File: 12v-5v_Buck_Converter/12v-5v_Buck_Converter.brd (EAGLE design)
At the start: 44 x 35.2 mm, 22 parts, among them J1 PJ-037A, U1 ZXMN3A01Z, U2 TERMINAL_BLOCK_2P, U3 TERMINAL_BLOCK_2P, U4 TERMINAL_BLOCK_2P, U5 TERMINAL_BLOCK_2P, U6 RT7258GSP

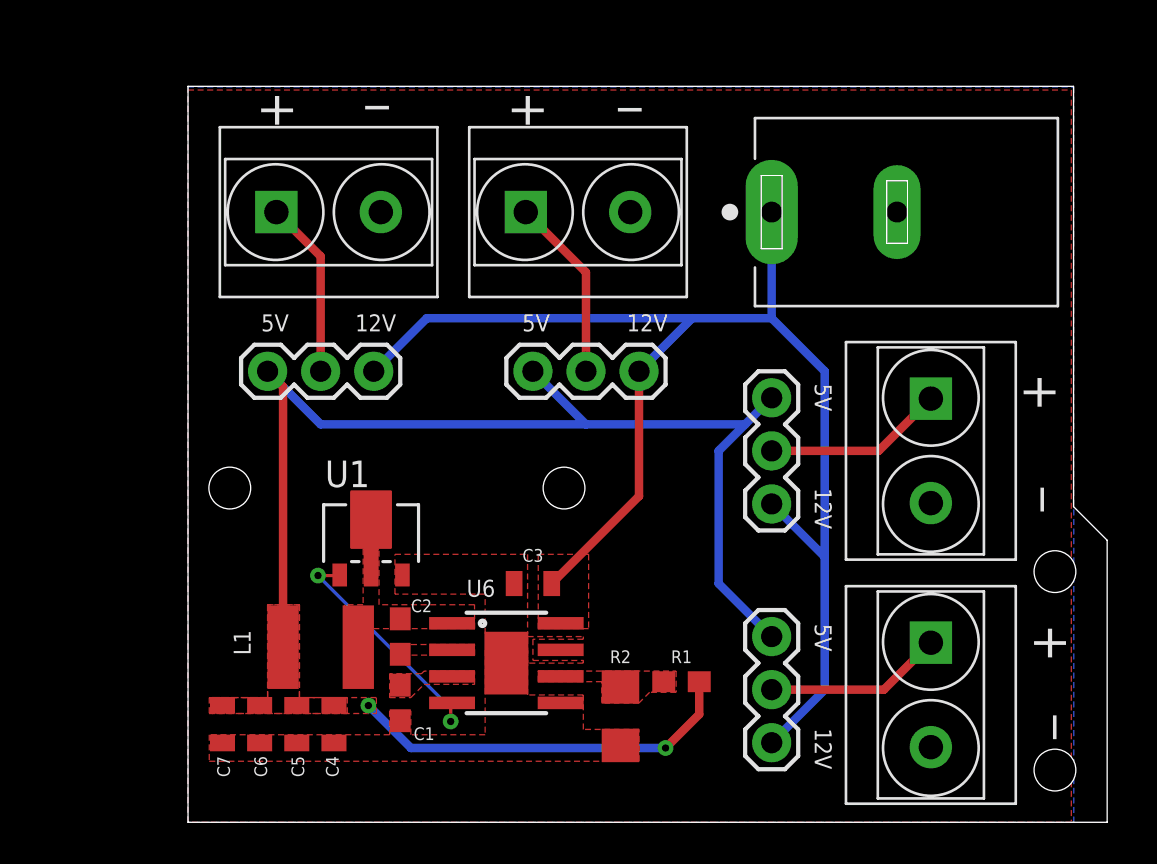
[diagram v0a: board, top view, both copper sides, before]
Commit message: Redesign to fix incorrect specs
MOSFET needed to have a Vgs of 5V and all of the other passive components were adjusted to be more temperature/current compatible
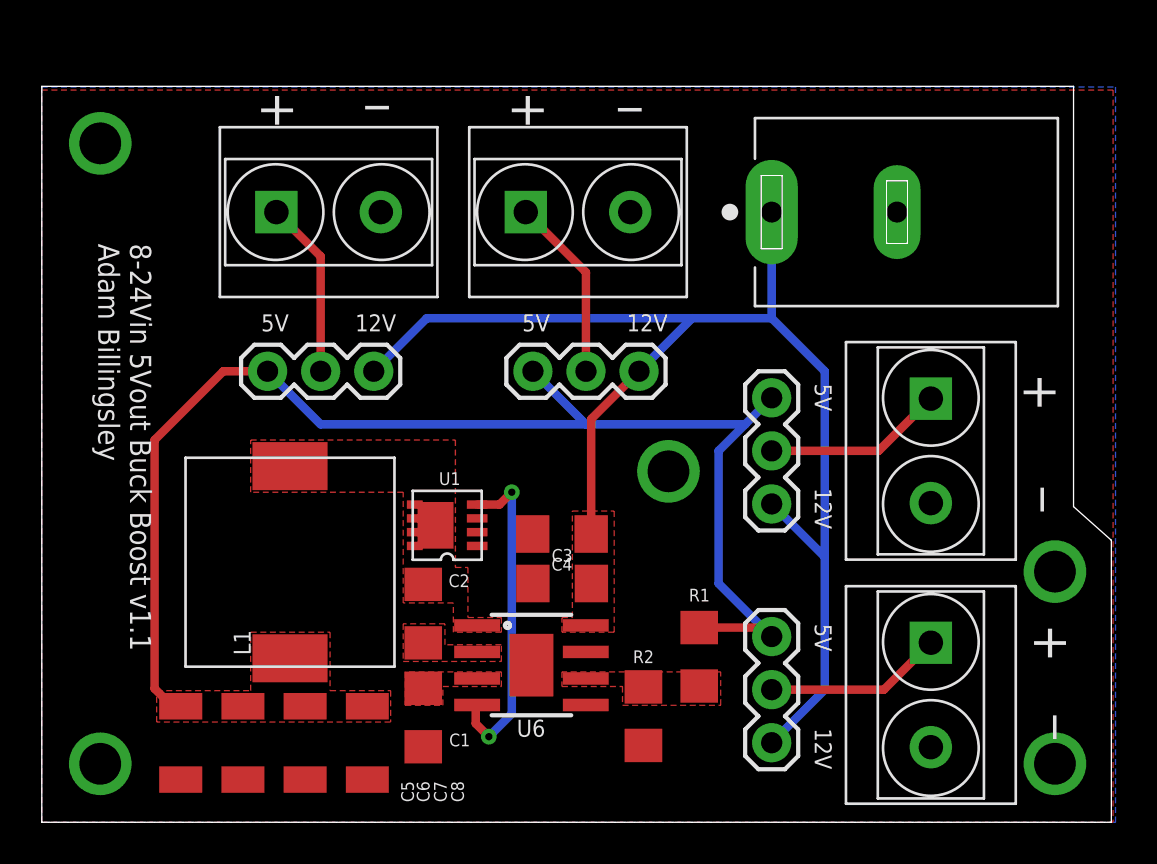
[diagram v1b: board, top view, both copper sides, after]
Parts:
- added C8: 22uF, Adam's Parts (work):1210
- C1, C2: device Adam's Parts (work):0603-CAPACITOR -> Adam's Parts (work):1206-CAPACITOR
- C3, C4: value 22uF -> 10uF; device Adam's Parts (work):0805 -> Adam's Parts (work):1206-CAPACITOR
- C5, C6, C7: device Adam's Parts (work):0805 -> Adam's Parts (work):1210
- L1: value 10uH -> 4.7uH; device Adam's Parts (work):INDUCTOR_LSXND5050YAL100MMG -> Adam's Parts (work):INDUCTOR-7443330470
- R1: value 82k -> 93.1k; device Adam's Parts (work):0603 -> Adam's Parts (work):1206-CAPACITOR
- R2: value 16k -> 18k; device Adam's Parts (work):1206 -> Adam's Parts (work):1206-CAPACITOR
- U1: device Adam's Parts (work):SOT89-R -> Adam's Parts (work):SI7114DN
- moved C4 14.2 mm to (17.9, 13.8), turned to 180 degrees
- moved FRAME1 7.00 mm to (14.0, -8.00)
- moved U1 5.86 mm to (14.3, 15.4), turned to 180 degrees
- moved L1 4.32 mm to (4.88, 12.4), turned to 90 degrees
- moved C5 3.50 mm to (8.59, 3.80)
- moved C6 2.36 mm to (5.61, 3.80)
- moved C2 1.56 mm to (11.3, 9.99)
- moved R1 1.46 mm to (24.5, 7.92), turned to 90 degrees
- moved C3 1.40 mm to (17.9, 11.4)
- moved C7 1.33 mm to (2.63, 3.80)
- moved C1 1.30 mm to (11.3, 5.01)
- moved U6 1.20 mm to (16.4, 7.52)
- moved R2 1.10 mm to (21.8, 5.08)
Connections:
- net 12V: now also C4.1
- net 5V: now also C8.1, L1.2; no longer C4.1, L1.P$2
- net BG: now also U1.4; no longer U1.2
- net GND: now also C8.2, U1.2, U1.3
- net SW: now also L1.1, U1.5, U1.6, U1.7, U1.8, U1.9; no longer L1.P$1, U1.3
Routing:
- net 5V: track 73.5 -> 65.0 mm, vias 2 -> 0
- net BG: track 11.6 -> 15.9 mm
- net 12V: track 66.7 -> 63.5 mm
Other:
- board size 44 x 35.2 mm -> 51.2 x 35.2 mm
- board text added: "8-24Vin 5Vout Buck Boost v1.1 Adam Billingsley"
- board text removed: "12Vin 5Vout Buck Boost v1.0 Adam Billingsley"

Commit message: updated buck converter, added shift register boards
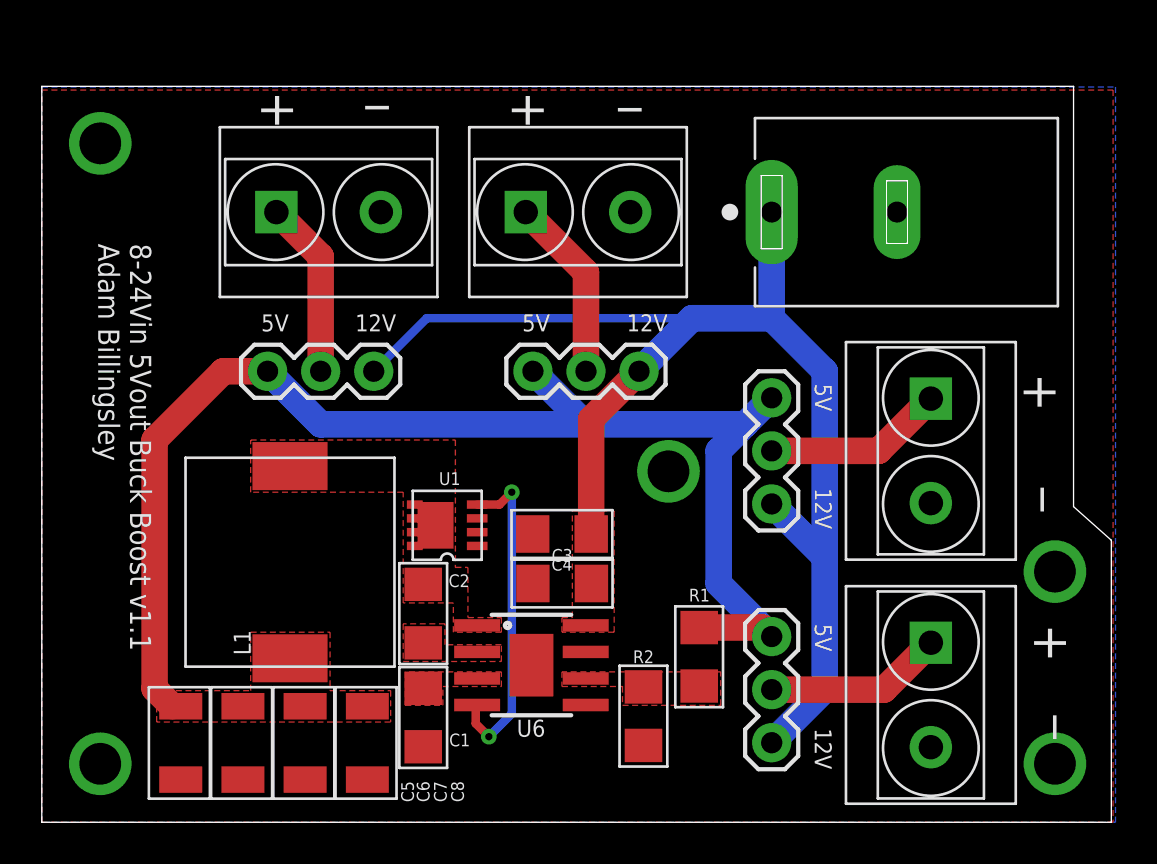
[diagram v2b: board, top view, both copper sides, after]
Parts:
- flipped FRAME1 to the bottom
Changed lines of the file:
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@@
 <layer number="27" name="tValues" color="7" fill="1" visible="yes" active="yes"/>
 <layer number="28" name="bValues" color="7" fill="1" visible="yes" active="yes"/>
-<layer number="29" name="tStop" color="7" fill="3" visible="no" active="yes"/>
-<layer number="30" name="bStop" color="7" fill="6" visible="no" active="yes"/>
-<layer number="31" name="tCream" color="7" fill="4" visible="no" active="yes"/>
-<layer number="32" name="bCream" color="7" fill="5" visible="no" active="yes"/>
-<layer number="33" name="tFinish" color="6" fill="3" visible="no" active="yes"/>
+<layer number="29" name="tStop" color="7" fill="3" visible="yes" active="yes"/>
+<layer number="30" name="bStop" color="7" fill="6" visible="yes" active="yes"/>
+<layer number="31" name="tCream" color="7" fill="4" visible="yes" active="yes"/>
+<layer number="32" name="bCream" color="7" fill="5" visible="yes" active="yes"/>
+<layer number="33" name="tFinish" color="6" fill="3" visible="yes" active="yes"/>
 <layer number="34" name="bFinish" color="6" fill="6" visible="no" active="yes"/>
 <layer number="35" name="tGlue" color="7" fill="4" visible="no" active="yes"/>
@@
 <attribute name="VALUE" x="17.9" y="14.943" size="0.6096" layer="27" font="vector" ratio="20" rot="R180" align="top-center"/>
 </element>
-<element name="FRAME1" library="SparkFun-Aesthetics" library_urn="urn:adsk.eagle:library:507" package="CREATIVE_COMMONS" package3d_urn="urn:adsk.eagle:package:37121/1" value="FRAME-LETTER" x="14" y="-8" smashed="yes"/>
+<element name="FRAME1" library="SparkFun-Aesthetics" library_urn="urn:adsk.eagle:library:507" package="CREATIVE_COMMONS" package3d_urn="urn:adsk.eagle:package:37121/1" value="FRAME-LETTER" x="14" y="-8" smashed="yes" rot="MR0"/>
 </elements>
 <signals>
@@
 <contactref element="JP4" pad="3"/>
 <contactref element="JP3" pad="3"/>
-<wire x1="27.94" y1="20.32" x2="26.67" y2="19.05" width="0.4064" layer="16"/>
-<wire x1="6.35" y1="19.05" x2="3.81" y2="21.59" width="0.4064" layer="16"/>
-<wire x1="26.67" y1="19.05" x2="19.05" y2="19.05" width="0.4064" layer="16"/>
-<wire x1="19.05" y1="19.05" x2="6.35" y2="19.05" width="0.4064" layer="16"/>
-<wire x1="16.51" y1="21.59" x2="19.05" y2="19.05" width="0.4064" layer="16"/>
-<wire x1="27.94" y1="8.89" x2="25.4" y2="11.43" width="0.4064" layer="16"/>
-<wire x1="25.4" y1="11.43" x2="25.4" y2="17.78" width="0.4064" layer="16"/>
-<wire x1="25.4" y1="17.78" x2="26.67" y2="19.05" width="0.4064" layer="16"/>
+<wire x1="27.94" y1="20.32" x2="26.67" y2="19.05" width="1.27" layer="16"/>
+<wire x1="6.35" y1="19.05" x2="3.81" y2="21.59" width="1.27" layer="16"/>
+<wire x1="26.67" y1="19.05" x2="19.05" y2="19.05" width="1.27" layer="16"/>
+<wire x1="19.05" y1="19.05" x2="6.35" y2="19.05" width="1.27" layer="16"/>
+<wire x1="16.51" y1="21.59" x2="19.05" y2="19.05" width="1.27" layer="16"/>
+<wire x1="27.94" y1="8.89" x2="25.4" y2="11.43" width="1.27" layer="16"/>
+<wire x1="25.4" y1="11.43" x2="25.4" y2="17.78" width="1.27" layer="16"/>
+<wire x1="25.4" y1="17.78" x2="26.67" y2="19.05" width="1.27" layer="16"/>
 <polygon width="0.1524" layer="1" thermals="no">
 <vertex x="-1.5" y="4.8"/>
@@
 <vertex x="9.7" y="4.8"/>
 </polygon>
-<wire x1="3.81" y1="21.59" x2="1.69" y2="21.59" width="0.4064" layer="1"/>
-<wire x1="1.69" y1="21.59" x2="-1.6" y2="18.3" width="0.4064" layer="1"/>
-<wire x1="-1.6" y1="18.3" x2="-1.6" y2="6.4" width="0.4064" layer="1"/>
-<wire x1="-1.6" y1="6.4" x2="-0.754" y2="5.554" width="0.4064" layer="1"/>
+<wire x1="3.81" y1="21.59" x2="1.69" y2="21.59" width="1.27" layer="1"/>
+<wire x1="1.69" y1="21.59" x2="-1.6" y2="18.3" width="1.27" layer="1"/>
+<wire x1="-1.6" y1="18.3" x2="-1.6" y2="6.4" width="1.27" layer="1"/>
+<wire x1="-1.6" y1="6.4" x2="-0.754" y2="5.554" width="1.27" layer="1"/>
 <wire x1="-0.754" y1="5.554" x2="-0.349" y2="5.554" width="0.4064" layer="1"/>
-<wire x1="24.469" y1="9.322" x2="27.508" y2="9.322" width="0.4064" layer="1"/>
-<wire x1="27.508" y1="9.322" x2="27.94" y2="8.89" width="0.4064" layer="1"/>
+<wire x1="24.469" y1="9.322" x2="27.508" y2="9.322" width="1.27" layer="1"/>
+<wire x1="27.508" y1="9.322" x2="27.94" y2="8.89" width="1.27" layer="1"/>
 </signal>
 <signal name="BG">
@@
 <contactref element="JP3" pad="1"/>
 <contactref element="JP4" pad="1"/>
-<wire x1="27.94" y1="15.24" x2="30.48" y2="12.7" width="0.4064" layer="16"/>
-<wire x1="30.48" y1="6.35" x2="27.94" y2="3.81" width="0.4064" layer="16"/>
-<wire x1="30.48" y1="12.7" x2="30.48" y2="6.35" width="0.4064" layer="16"/>
-<wire x1="30.48" y1="12.7" x2="30.48" y2="21.59" width="0.4064" layer="16"/>
-<wire x1="30.48" y1="21.59" x2="27.94" y2="24.13" width="0.4064" layer="16"/>
-<wire x1="27.94" y1="24.13" x2="24.13" y2="24.13" width="0.4064" layer="16"/>
-<wire x1="24.13" y1="24.13" x2="21.59" y2="21.59" width="0.4064" layer="16"/>
-<wire x1="27.94" y1="29.21" x2="27.94" y2="24.13" width="0.4064" layer="16"/>
+<wire x1="27.94" y1="15.24" x2="30.48" y2="12.7" width="1.27" layer="16"/>
+<wire x1="30.48" y1="6.35" x2="27.94" y2="3.81" width="1.27" layer="16"/>
+<wire x1="30.48" y1="12.7" x2="30.48" y2="6.35" width="1.27" layer="16"/>
+<wire x1="30.48" y1="12.7" x2="30.48" y2="21.59" width="1.27" layer="16"/>
+<wire x1="30.48" y1="21.59" x2="27.94" y2="24.13" width="1.27" layer="16"/>
+<wire x1="27.94" y1="24.13" x2="24.13" y2="24.13" width="1.27" layer="16"/>
+<wire x1="24.13" y1="24.13" x2="21.59" y2="21.59" width="1.27" layer="16"/>
+<wire x1="27.94" y1="29.21" x2="27.94" y2="24.13" width="1.27" layer="16"/>
 <wire x1="24.13" y1="24.13" x2="11.43" y2="24.13" width="0.4064" layer="16"/>
 <wire x1="11.43" y1="24.13" x2="8.89" y2="21.59" width="0.4064" layer="16"/>
@@
 <vertex x="20.4" y="9.1"/>
 </polygon>
-<wire x1="19.3" y1="13.8" x2="19.3" y2="19.3" width="0.4064" layer="1"/>
-<wire x1="19.3" y1="19.3" x2="21.59" y2="21.59" width="0.4064" layer="1"/>
+<wire x1="19.3" y1="13.8" x2="19.3" y2="19.3" width="1.27" layer="1"/>
+<wire x1="19.3" y1="19.3" x2="21.59" y2="21.59" width="1.27" layer="1"/>
 </signal>
 <signal name="N$1">
@@
 <contactref element="JP4" pad="2"/>
 <contactref element="U5" pad="1"/>
-<wire x1="6.35" y1="27.091" x2="4.231" y2="29.21" width="0.4064" layer="1"/>
-<wire x1="6.35" y1="21.59" x2="6.35" y2="27.091" width="0.4064" layer="1"/>
+<wire x1="6.35" y1="27.091" x2="4.231" y2="29.21" width="1.27" layer="1"/>
+<wire x1="6.35" y1="21.59" x2="6.35" y2="27.091" width="1.27" layer="1"/>
 </signal>
 <signal name="N$3">
 <contactref element="U4" pad="1"/>
 <contactref element="JP3" pad="2"/>
-<wire x1="19.05" y1="26.329" x2="16.169" y2="29.21" width="0.4064" layer="1"/>
-<wire x1="19.05" y1="21.59" x2="19.05" y2="26.329" width="0.4064" layer="1"/>
+<wire x1="19.05" y1="26.329" x2="16.169" y2="29.21" width="1.27" layer="1"/>
+<wire x1="19.05" y1="21.59" x2="19.05" y2="26.329" width="1.27" layer="1"/>
 </signal>
 <signal name="N$4">
 <contactref element="U3" pad="1"/>
 <contactref element="JP2" pad="2"/>
-<wire x1="33.06" y1="17.78" x2="35.56" y2="20.28" width="0.4064" layer="1"/>
-<wire x1="27.94" y1="17.78" x2="33.06" y2="17.78" width="0.4064" layer="1"/>
+<wire x1="33.06" y1="17.78" x2="35.56" y2="20.28" width="1.27" layer="1"/>
+<wire x1="27.94" y1="17.78" x2="33.06" y2="17.78" width="1.27" layer="1"/>
 </signal>
 <signal name="N$5">
 <contactref element="U2" pad="1"/>
 <contactref element="JP1" pad="2"/>
-<wire x1="33.314" y1="6.35" x2="35.56" y2="8.596" width="0.4064" layer="1"/>
-<wire x1="27.94" y1="6.35" x2="33.314" y2="6.35" width="0.4064" layer="1"/>
+<wire x1="33.314" y1="6.35" x2="35.56" y2="8.596" width="1.27" layer="1"/>
+<wire x1="27.94" y1="6.35" x2="33.314" y2="6.35" width="1.27" layer="1"/>
 </signal>
 <signal name="N$8">
